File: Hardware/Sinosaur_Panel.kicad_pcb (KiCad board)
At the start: 2 copper layers, 60.8 x 128.5 mm, 31 parts

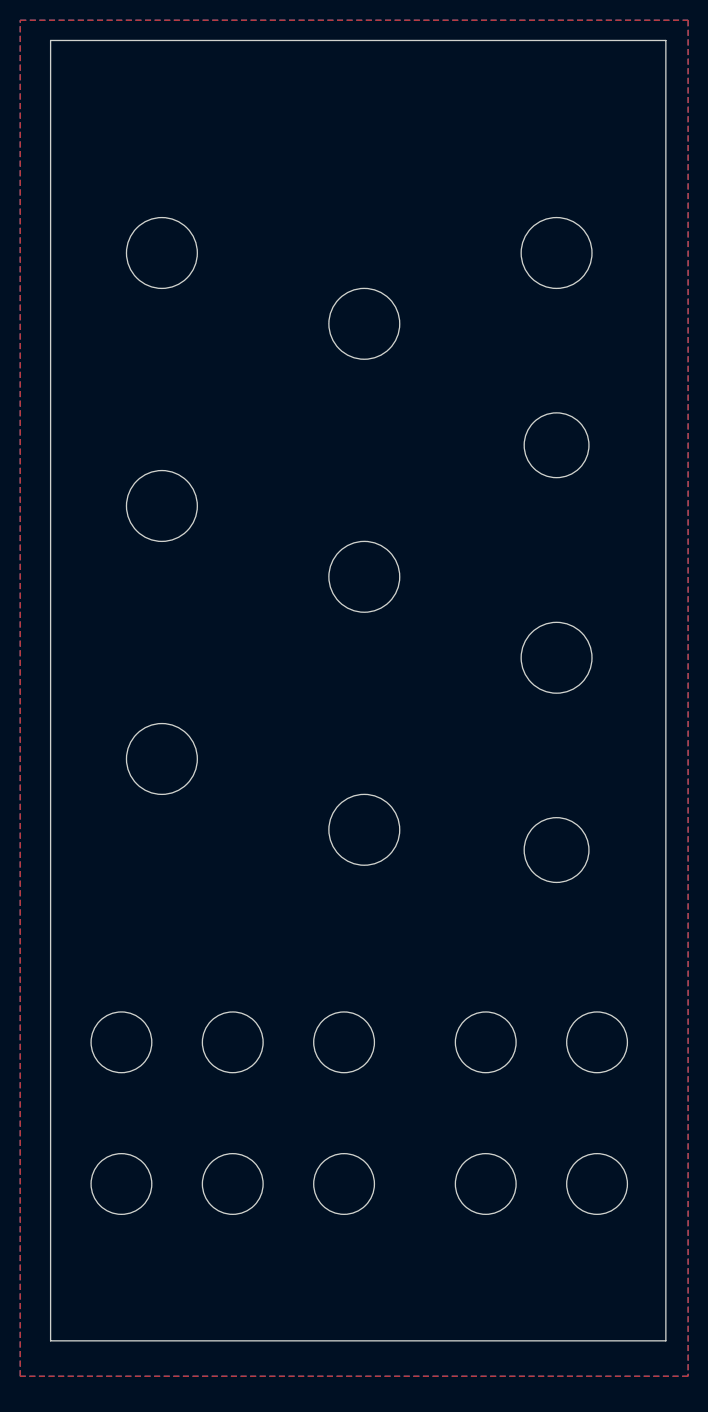
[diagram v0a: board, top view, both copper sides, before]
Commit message: Started laying out control board
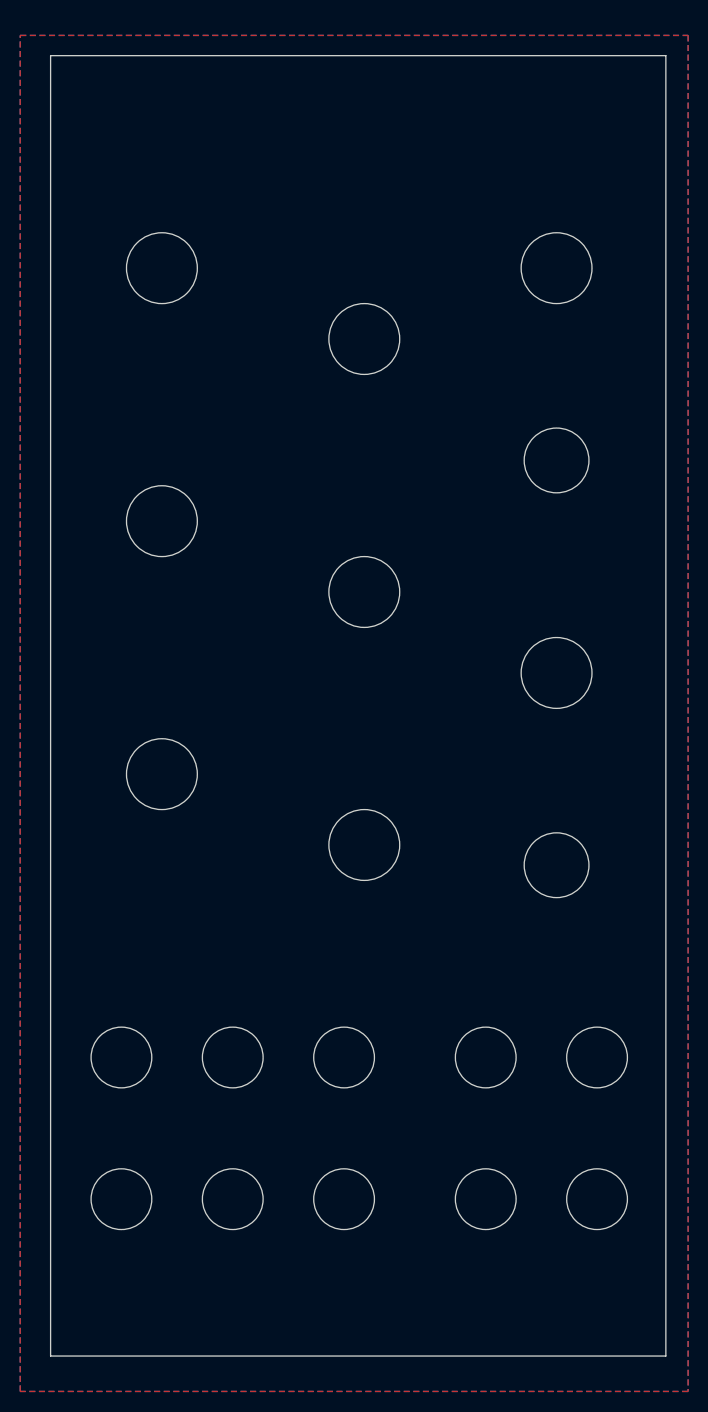
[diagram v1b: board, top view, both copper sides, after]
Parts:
- moved Ref** 1.50 mm to (149.6, 101.8)
- moved Ref** 1.50 mm to (117.6, 153.8)
- moved Ref** 1.50 mm to (149.6, 61.8)
- moved Ref** 1.50 mm to (153.6, 153.8)
- moved Ref** 1.50 mm to (128.6, 153.8)
- moved Ref** 1.50 mm to (107.1, 166.3)
- moved Ref** 1.50 mm to (152.9, 166.3)
- moved Ref** 1.50 mm to (110.6, 61.8)
- moved Ref** 1.50 mm to (153.6, 139.8)
- moved Ref** 1.50 mm to (110.6, 111.8)
- moved Ref** 1.50 mm to (149.6, 80.8)
- moved Ref** 1.50 mm to (142.6, 139.8)
- moved Ref** 1.50 mm to (130.6, 118.8)
- moved Ref** 1.50 mm to (142.6, 153.8)
- moved Ref** 1.50 mm to (107.1, 43.8)
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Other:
- board text added: "Mountjoy Modular 2024 Sinosaur Panel v1.0"
- board text removed: "1"
- board text removed: "Mountjoy Modular 2024 Kishoof Panel v1.0"

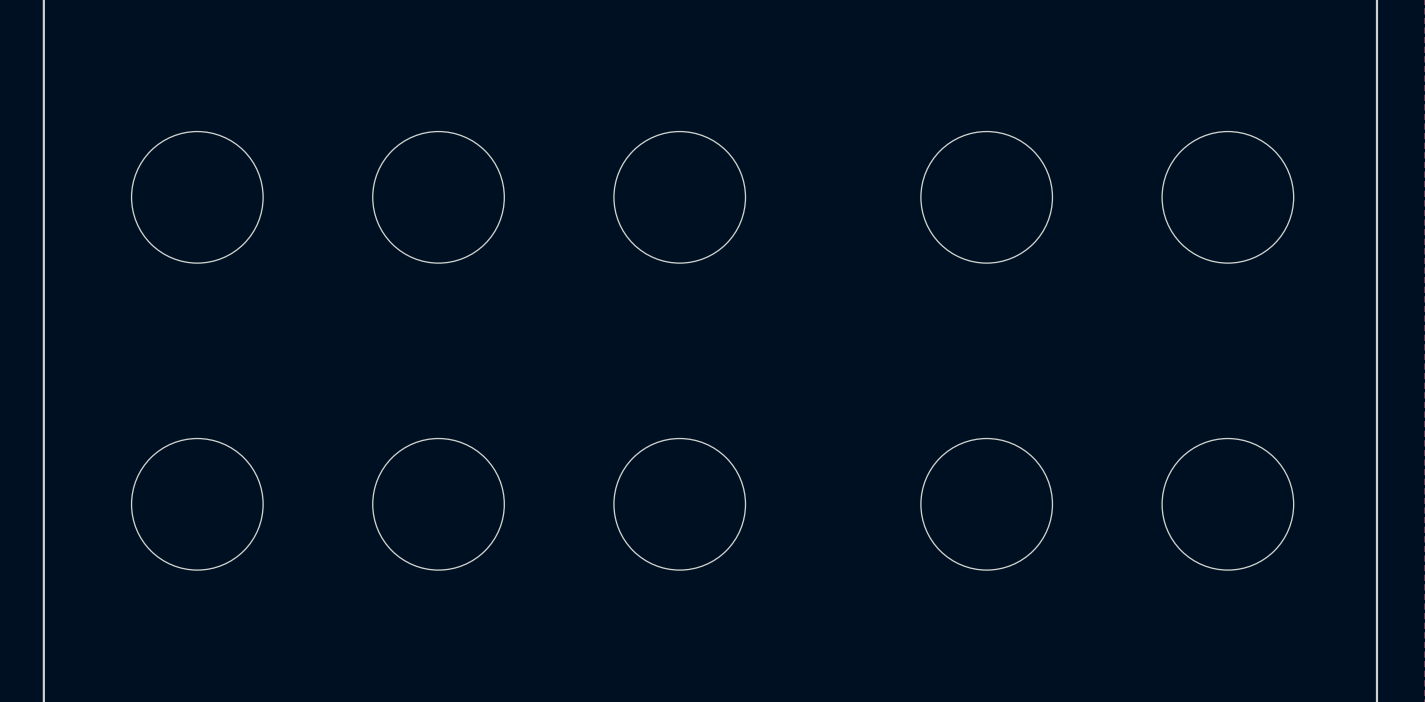
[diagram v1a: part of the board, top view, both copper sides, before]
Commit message: Started control layout
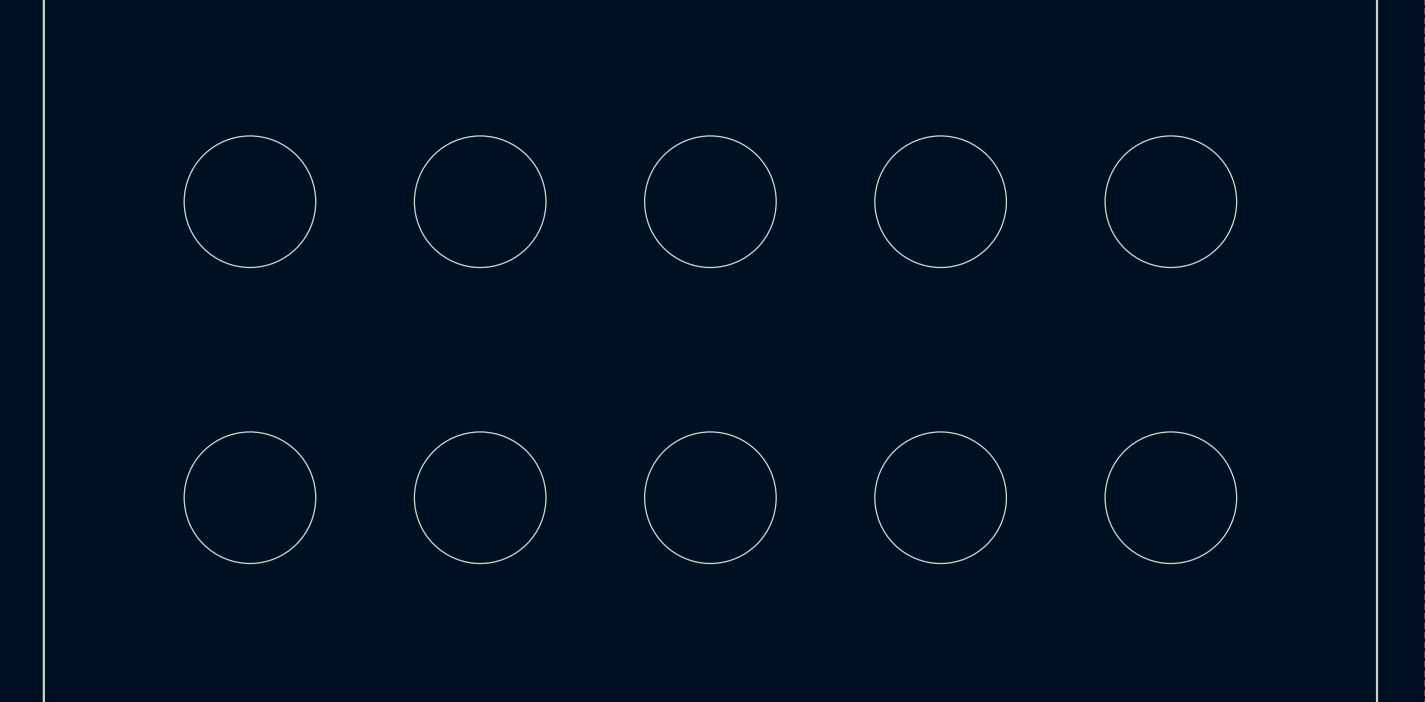
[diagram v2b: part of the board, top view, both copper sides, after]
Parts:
- moved Ref** 2.62 mm to (151.0, 153.5)
- moved Ref** 2.61 mm to (151.0, 140.0)
- moved Ref** 2.42 mm to (109.0, 153.5)
- moved kibuzzard-666C296D 2.42 mm to (109.0, 147.0)
- moved Ref** 2.41 mm to (109.0, 140.0)
- moved Ref** 2.12 mm to (140.5, 153.5)
- moved Ref** 2.11 mm to (140.5, 140.0)
- moved Ref** 1.92 mm to (119.5, 153.5)
- moved Ref** 1.91 mm to (119.5, 140.0)
- moved kibuzzard-666C29A3 1.90 mm to (119.5, 146.7)
- moved Ref** 1.43 mm to (130.0, 153.5)
- moved Ref** 1.41 mm to (130.0, 140.0)
- moved kibuzzard-666C29AC 1.40 mm to (130.0, 146.7)
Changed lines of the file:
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@@
 	(footprint "Custom_Footprints:Thonkiconn_Socket_MountingHole_6mm"
 		(layer "F.Cu")
-		(at 142.6 139.8 180)
+		(at 140.5 140 180)
 		(descr "Mounting Hole 6mm, no annular")
 		(tags "mounting hole 6mm no annular")
@@
 			)
 		)
-		(property "Footprint" ""
+		(property "Footprint" "Custom_Footprints:Thonkiconn_Socket_MountingHole_6mm"
 			(at 0 0 180)
 			(unlocked yes)
@@
 			(size 6 6)
 			(drill 6)
-			(layers "F&B.Cu" "*.Mask")
+			(layers "*.Cu" "*.Mask")
 		)
 		(model "${CUSTOM_3D}/PJ301M-12 Thonkiconn v0.2.stp"
@@
 	(footprint "Custom_Footprints:Thonkiconn_Socket_MountingHole_6mm"
 		(layer "F.Cu")
-		(at 106.6 139.8 180)
+		(at 109 140 180)
 		(descr "Mounting Hole 6mm, no annular")
 		(tags "mounting hole 6mm no annular")
@@
 			)
 		)
-		(property "Footprint" ""
+		(property "Footprint" "Custom_Footprints:Thonkiconn_Socket_MountingHole_6mm"
 			(at 0 0 180)
 			(unlocked yes)
@@
 			(size 6 6)
 			(drill 6)
-			(layers "F&B.Cu" "*.Mask")
+			(layers "*.Cu" "*.Mask")
 		)
 		(model "${CUSTOM_3D}/PJ301M-12 Thonkiconn v0.2.stp"
@@
 	(footprint "kibuzzard-666C29AC"
 		(layer "F.Cu")
-		(at 128.6 146.7)
+		(at 130 146.7)
 		(descr "Generated with KiBuzzard")
 		(tags "kb_params=eyJBbGlnbm1lbnRDaG9pY2UiOiAiQ2VudGVyIiwgIkNhcExlZnRDaG9pY2UiOiAiWyIsICJDYXBSaWdodENob2ljZSI6ICJdIiwgIkZvbnRDb21ib0JveCI6ICJVYnVudHVNb25vLUIiLCAiSGVpZ2h0Q3RybCI6IDIuNSwgIkxheWVyQ29tYm9Cb3giOiAiRi5NYXNrIiwgIkxpbmVTcGFjaW5nQ3RybCI6IDEuNSwgIk11bHRpTGluZVRleHQiOiAiMyIsICJQYWRkaW5nQm90dG9tQ3RybCI6IDMuMCwgIlBhZGRpbmdMZWZ0Q3RybCI6IDMuMCwgIlBhZGRpbmdSaWdodEN0cmwiOiAyLjAsICJQYWRkaW5nVG9wQ3RybCI6IDMuMCwgIldpZHRoQ3RybCI6IDAuMCwgImFkdmFuY2VkQ2hlY2tib3giOiBmYWxzZSwgImlubGluZUZvcm1hdFRleHRib3giOiBmYWxzZSwgImxpbmVvdmVyU3R5bGVDaG9pY2UiOiAiU3F1YXJlIiwgImxpbmVvdmVyVGhpY2tuZXNzQ3RybCI6IDF9")
@@
 	(footprint "Custom_Footprints:Thonkiconn_Socket_MountingHole_6mm"
 		(layer "F.Cu")
-		(at 117.6 139.8 180)
+		(at 119.5 140 180)
 		(descr "Mounting Hole 6mm, no annular")
 		(tags "mounting hole 6mm no annular")
@@
 			)
 		)
-		(property "Footprint" ""
+		(property "Footprint" "Custom_Footprints:Thonkiconn_Socket_MountingHole_6mm"
 			(at 0 0 180)
 			(unlocked yes)
@@
 			(size 6 6)
 			(drill 6)
-			(layers "F&B.Cu" "*.Mask")
+			(layers "*.Cu" "*.Mask")
 		)
 		(model "${CUSTOM_3D}/PJ301M-12 Thonkiconn v0.2.stp"
@@
 	(footprint "Custom_Footprints:Thonkiconn_Socket_MountingHole_6mm"
 		(layer "F.Cu")
-		(at 106.6 153.8 180)
+		(at 109 153.5 180)
 		(descr "Mounting Hole 6mm, no annular")
 		(tags "mounting hole 6mm no annular")
@@
 			)
 		)
-		(property "Footprint" ""
+		(property "Footprint" "Custom_Footprints:Thonkiconn_Socket_MountingHole_6mm"
 			(at 0 0 180)
 			(unlocked yes)
@@
 			(size 6 6)
 			(drill 6)
-			(layers "F&B.Cu" "*.Mask")
+			(layers "*.Cu" "*.Mask")
 		)
 		(model "${CUSTOM_3D}/PJ301M-12 Thonkiconn v0.2.stp"
@@
 	(footprint "Custom_Footprints:Thonkiconn_Socket_MountingHole_6mm"
 		(layer "F.Cu")
-		(at 128.6 139.8 180)
+		(at 130 140 180)
 		(descr "Mounting Hole 6mm, no annular")
 		(tags "mounting hole 6mm no annular")
@@
 			)
 		)
-		(property "Footprint" ""
+		(property "Footprint" "Custom_Footprints:Thonkiconn_Socket_MountingHole_6mm"
 			(at 0 0 180)
 			(unlocked yes)
@@
 			(size 6 6)
 			(drill 6)
-			(layers "F&B.Cu" "*.Mask")
+			(layers "*.Cu" "*.Mask")
 		)
 		(model "${CUSTOM_3D}/PJ301M-12 Thonkiconn v0.2.stp"
@@
 	(footprint "Custom_Footprints:Thonkiconn_Socket_MountingHole_6mm"
 		(layer "F.Cu")
-		(at 117.6 153.8 180)
+		(at 119.5 153.5 180)
 		(descr "Mounting Hole 6mm, no annular")
 		(tags "mounting hole 6mm no annular")
@@
 			)
 		)
-		(property "Footprint" ""
+		(property "Footprint" "Custom_Footprints:Thonkiconn_Socket_MountingHole_6mm"
 			(at 0 0 180)
 			(unlocked yes)
@@
 	(footprint "Custom_Footprints:Thonkiconn_Socket_MountingHole_6mm"
 		(layer "F.Cu")
-		(at 153.6 153.8 180)
+		(at 151 153.5 180)
 		(descr "Mounting Hole 6mm, no annular")
 		(tags "mounting hole 6mm no annular")
@@
 			)
 		)
-		(property "Footprint" ""
+		(property "Footprint" "Custom_Footprints:Thonkiconn_Socket_MountingHole_6mm"
 			(at 0 0 180)
 			(unlocked yes)
@@
 			(size 6 6)
 			(drill 6)
-			(layers "F&B.Cu" "*.Mask")
+			(layers "*.Cu" "*.Mask")
 		)
 		(model "${CUSTOM_3D}/PJ301M-12 Thonkiconn v0.2.stp"
@@
 	(footprint "Custom_Footprints:Thonkiconn_Socket_MountingHole_6mm"
 		(layer "F.Cu")
-		(at 128.6 153.8 180)
+		(at 130 153.5 180)
 		(descr "Mounting Hole 6mm, no annular")
 		(tags "mounting hole 6mm no annular")
@@
 			)
 		)
-		(property "Footprint" ""
+		(property "Footprint" "Custom_Footprints:Thonkiconn_Socket_MountingHole_6mm"
 			(at 0 0 180)
 			(unlocked yes)
@@
 			(size 6 6)
 			(drill 6)
-			(layers "F&B.Cu" "*.Mask")
+			(layers "*.Cu" "*.Mask")
 		)
 		(model "${CUSTOM_3D}/PJ301M-12 Thonkiconn v0.2.stp"
@@
 	(footprint "kibuzzard-666C296D"
 		(layer "F.Cu")
-		(at 106.6 146.7)
+		(at 109 147)
 		(descr "Generated with KiBuzzard")
 		(tags "kb_params=eyJBbGlnbm1lbnRDaG9pY2UiOiAiQ2VudGVyIiwgIkNhcExlZnRDaG9pY2UiOiAiWyIsICJDYXBSaWdodENob2ljZSI6ICJdIiwgIkZvbnRDb21ib0JveCI6ICJVYnVudHVNb25vLUIiLCAiSGVpZ2h0Q3RybCI6IDIuNSwgIkxheWVyQ29tYm9Cb3giOiAiRi5NYXNrIiwgIkxpbmVTcGFjaW5nQ3RybCI6IDEuNSwgIk11bHRpTGluZVRleHQiOiAiMSIsICJQYWRkaW5nQm90dG9tQ3RybCI6IDMuMCwgIlBhZGRpbmdMZWZ0Q3RybCI6IDMuMCwgIlBhZGRpbmdSaWdodEN0cmwiOiAyLjAsICJQYWRkaW5nVG9wQ3RybCI6IDMuMCwgIldpZHRoQ3RybCI6IDAuMCwgImFkdmFuY2VkQ2hlY2tib3giOiBmYWxzZSwgImlubGluZUZvcm1hdFRleHRib3giOiBmYWxzZSwgImxpbmVvdmVyU3R5bGVDaG9pY2UiOiAiU3F1YXJlIiwgImxpbmVvdmVyVGhpY2tuZXNzQ3RybCI6IDF9")
@@
 	(footprint "Custom_Footprints:Thonkiconn_Socket_MountingHole_6mm"
 		(layer "F.Cu")
-		(at 153.6 139.8 180)
+		(at 151 140 180)
 		(descr "Mounting Hole 6mm, no annular")
 		(tags "mounting hole 6mm no annular")
@@
 			)
 		)
-		(property "Footprint" ""
+		(property "Footprint" "Custom_Footprints:Thonkiconn_Socket_MountingHole_6mm"
 			(at 0 0 180)
 			(unlocked yes)
@@
 			(size 6 6)
 			(drill 6)
-			(layers "F&B.Cu" "*.Mask")
+			(layers "*.Cu" "*.Mask")
 		)
 		(model "${CUSTOM_3D}/PJ301M-12 Thonkiconn v0.2.stp"
@@
 	(footprint "kibuzzard-666C29A3"
 		(layer "F.Cu")
-		(at 117.6 146.7)
+		(at 119.5 146.7)
 		(descr "Generated with KiBuzzard")
 		(tags "kb_params=eyJBbGlnbm1lbnRDaG9pY2UiOiAiQ2VudGVyIiwgIkNhcExlZnRDaG9pY2UiOiAiWyIsICJDYXBSaWdodENob2ljZSI6ICJdIiwgIkZvbnRDb21ib0JveCI6ICJVYnVudHVNb25vLUIiLCAiSGVpZ2h0Q3RybCI6IDIuNSwgIkxheWVyQ29tYm9Cb3giOiAiRi5NYXNrIiwgIkxpbmVTcGFjaW5nQ3RybCI6IDEuNSwgIk11bHRpTGluZVRleHQiOiAiMiIsICJQYWRkaW5nQm90dG9tQ3RybCI6IDMuMCwgIlBhZGRpbmdMZWZ0Q3RybCI6IDMuMCwgIlBhZGRpbmdSaWdodEN0cmwiOiAyLjAsICJQYWRkaW5nVG9wQ3RybCI6IDMuMCwgIldpZHRoQ3RybCI6IDAuMCwgImFkdmFuY2VkQ2hlY2tib3giOiBmYWxzZSwgImlubGluZUZvcm1hdFRleHRib3giOiBmYWxzZSwgImxpbmVvdmVyU3R5bGVDaG9pY2UiOiAiU3F1YXJlIiwgImxpbmVvdmVyVGhpY2tuZXNzQ3RybCI6IDF9")
@@
 	(footprint "Custom_Footprints:Thonkiconn_Socket_MountingHole_6mm"
 		(layer "F.Cu")
-		(at 142.6 153.8 180)
+		(at 140.5 153.5 180)
 		(descr "Mounting Hole 6mm, no annular")
 		(tags "mounting hole 6mm no annular")
@@
 			)
 		)
-		(property "Footprint" ""
+		(property "Footprint" "Custom_Footprints:Thonkiconn_Socket_MountingHole_6mm"
 			(at 0 0 180)
 			(unlocked yes)
@@
 			(size 6 6)
 			(drill 6)
-			(layers "F&B.Cu" "*.Mask")
+			(layers "*.Cu" "*.Mask")
 		)
 		(model "${CUSTOM_3D}/PJ301M-12 Thonkiconn v0.2.stp"
@@
 	)
 	(gr_rect
-		(start 102.6 135.778175)
-		(end 110.6 143.778175)
+		(start 105 135.778175)
+		(end 113 143.778175)
 		(stroke
 			(width 2)
@@
 	)
 	(gr_rect
-		(start 113.6 149.778175)
-		(end 121.6 157.778175)
+		(start 115.5 149.778175)
+		(end 123.5 157.778175)
 		(stroke
 			(width 2)
@@
 	)
 	(gr_rect
-		(start 102.6 149.778175)
-		(end 110.6 157.778175)
+		(start 105 149.778175)
+		(end 113 157.778175)
 		(stroke
 			(width 2)
@@
 	)
 	(gr_rect
-		(start 124.6 135.778175)
-		(end 132.6 143.778175)
+		(start 126 135.778175)
+		(end 134 143.778175)
 		(stroke
 			(width 2)
@@
 	)
 	(gr_rect
-		(start 124.6 149.778175)
-		(end 132.6 157.778175)
+		(start 126 149.778175)
+		(end 134 157.778175)
 		(stroke
 			(width 2)
@@
 	)
 	(gr_rect
-		(start 138.6 149.778175)
-		(end 157.6 157.778175)
+		(start 136.5 149.778175)
+		(end 155.5 157.778175)
 		(stroke
 			(width 2)
@@
 	)
 	(gr_rect
-		(start 113.6 135.778175)
-		(end 121.6 143.778175)
+		(start 115.5 135.778175)
+		(end 123.5 143.778175)
 		(stroke
 			(width 2)
@@
 	)
 	(gr_rect
-		(start 100 50)
-		(end 160 160)
+		(start 101.4 50)
+		(end 161.4 160)
 		(stroke
 			(width 0.1)
@@
 	)
 	(gr_text "GATE"
-		(at 153.6 134.778175 0)
+		(at 151 134.778175 0)
 		(layer "F.Mask")
 		(effects
@@
 	)
 	(gr_text "Sine"
-		(at 117.6 161.778175 0)
+		(at 119 161.778175 0)
 		(layer "F.Mask")
 		(effects
@@
 	)
 	(gr_text "CLK"
-		(at 142.6 134.778175 0)
+		(at 140.5 134.778175 0)
 		(layer "F.Mask")
 		(effects
@@
 	)
 	(gr_text "Swell"
-		(at 153.6 161.778175 0)
+		(at 151 161.778175 0)
 		(layer "F.Mask")
 		(effects
@@
 	)
 	(gr_text "Ramp"
-		(at 142.6 161.778175 0)
+		(at 140.5 161.778175 0)
 		(layer "F.Mask")
 		(effects
